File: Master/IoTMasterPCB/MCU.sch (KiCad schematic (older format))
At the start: 34 parts

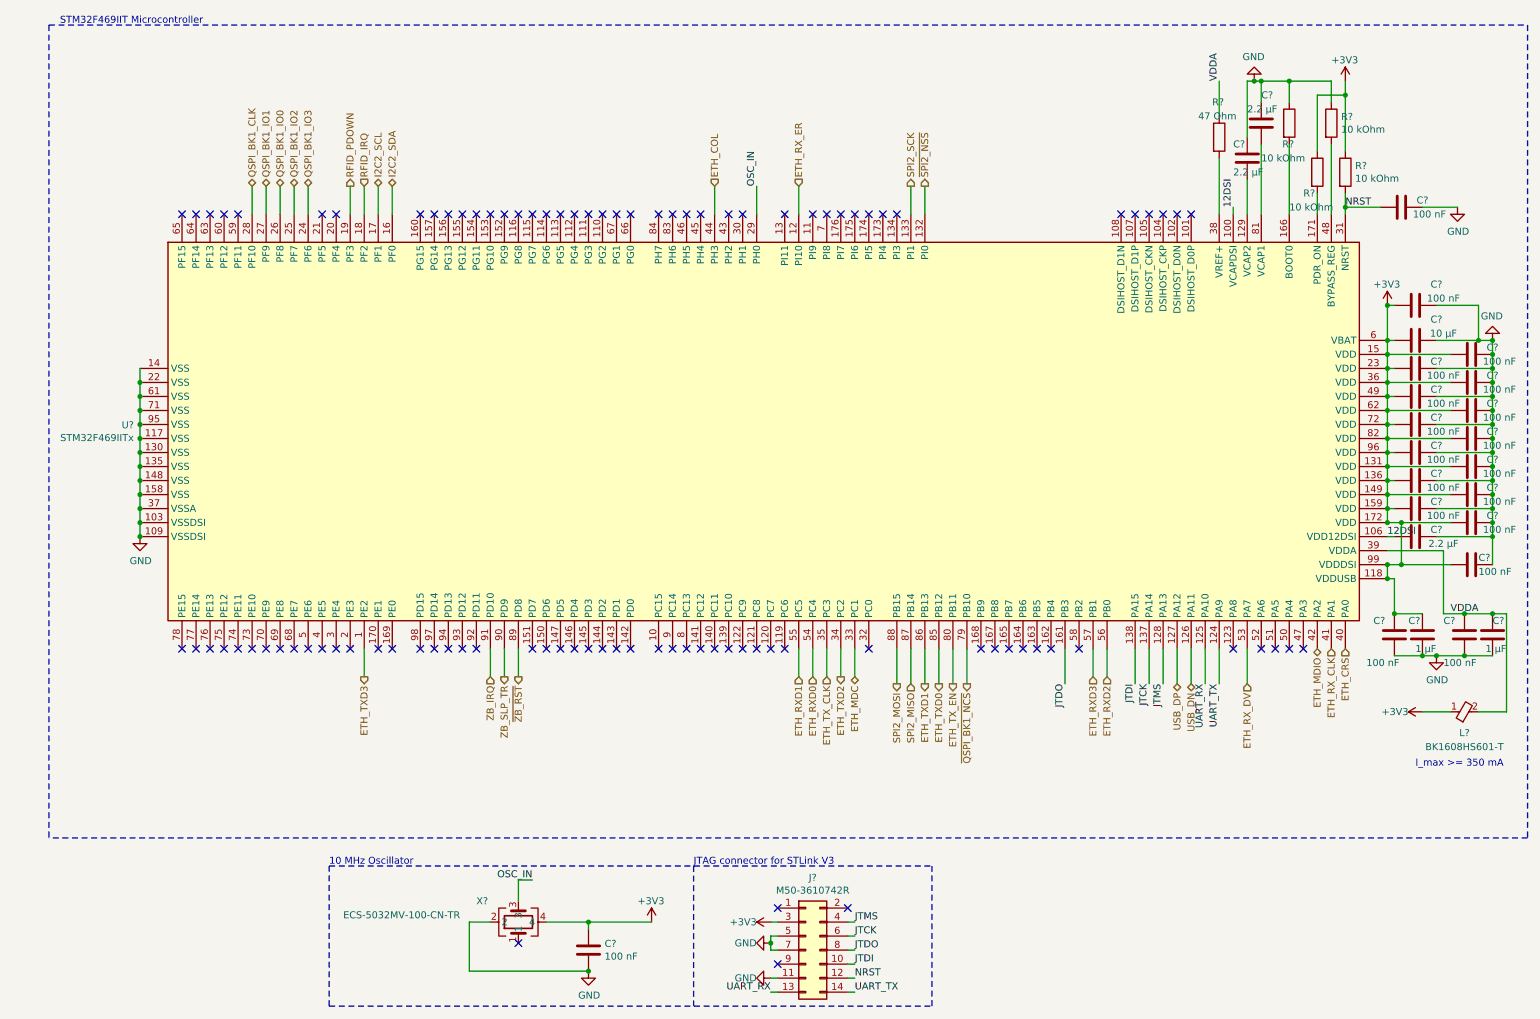
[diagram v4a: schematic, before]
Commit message: Finished RFID and Ethernet circuits.
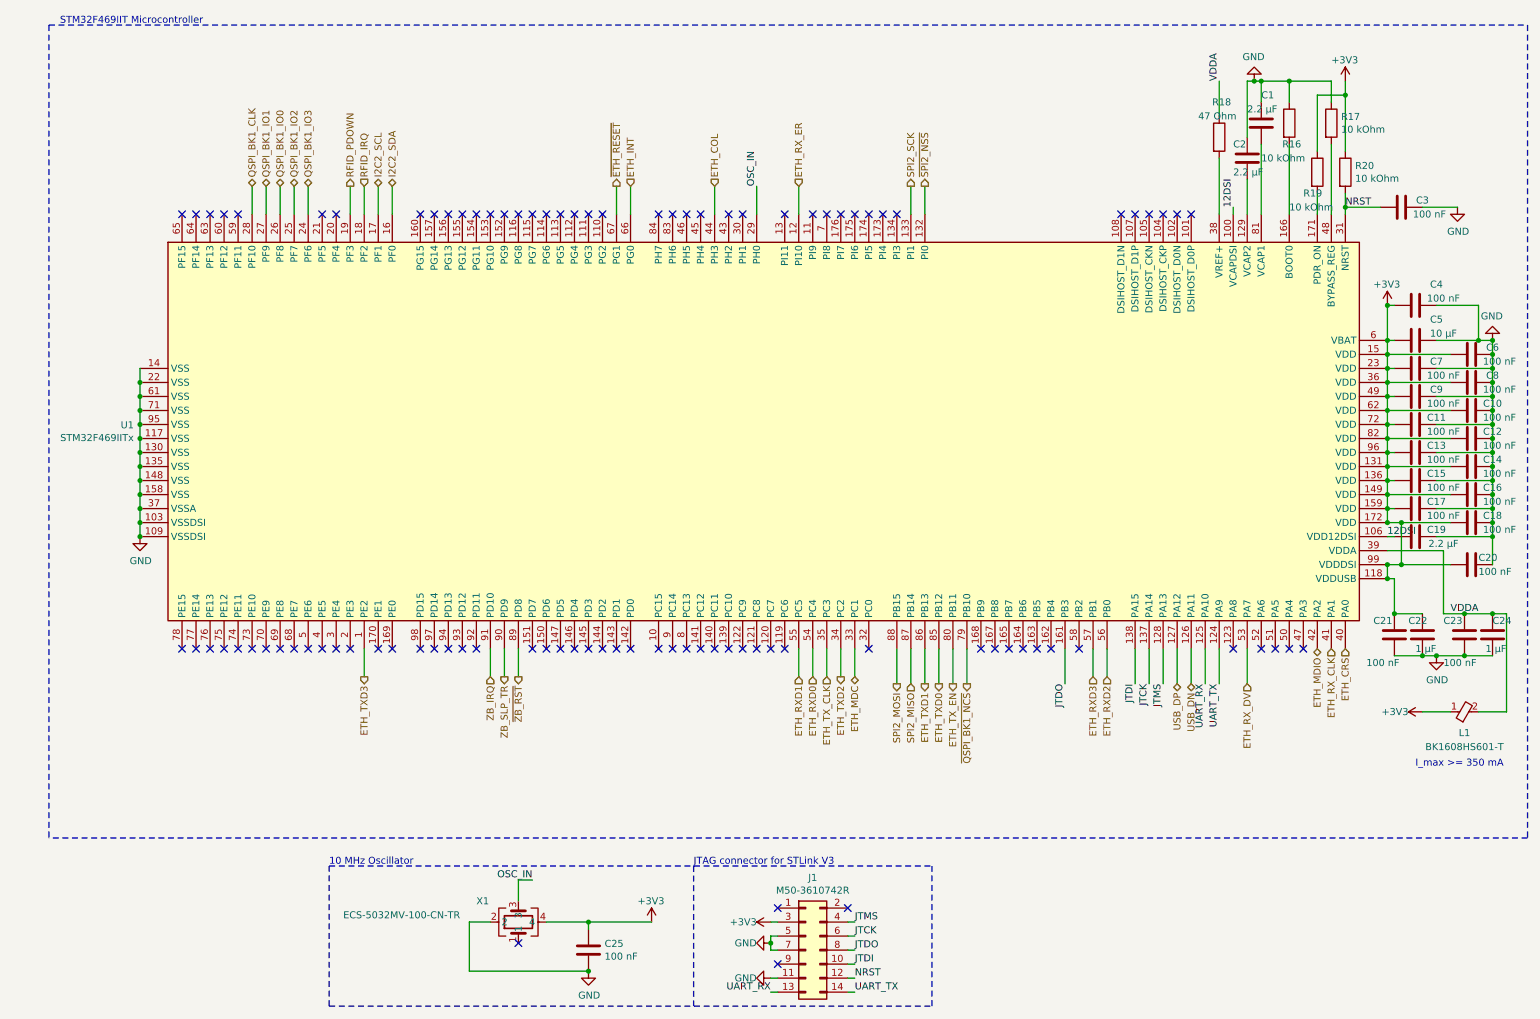
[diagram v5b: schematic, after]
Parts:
- L1: renamed from L?; Height 0.95 -> (none); Manufacturer_Name TAIYO YUDEN -> (none); Manufacturer_Part_Number BK1608HS601-T -> (none); Mouser Part Number 963-BK1608HS601-T -> (none); Mouser Price/Stock https://www.mouser.co.uk/ProductDetail/Taiyo-Yuden/BK1608HS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 -> (none)
- gave numbers to parts that had none: 33
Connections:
- net ETH_INT: now reaches U1.66 (PG0)
- net ~ETH_RESET: now reaches U1.67 (PG1)
- no-connect marks 98 -> 96

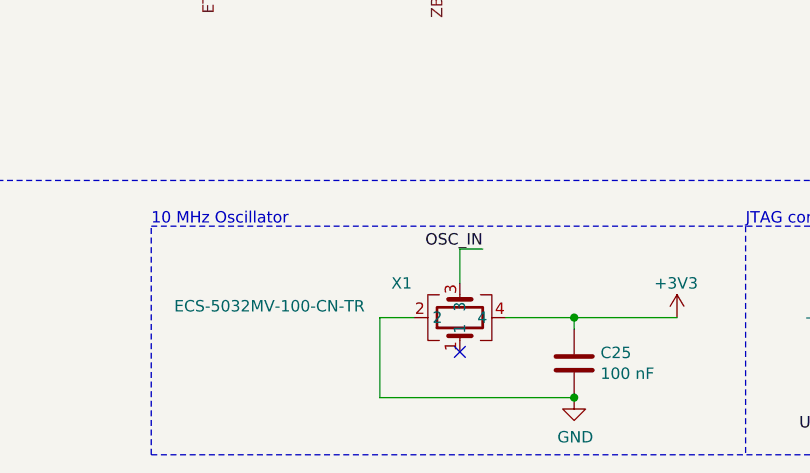
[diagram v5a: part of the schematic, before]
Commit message: Minor changes to schematic, finished placing all components, only minor fixes needed to PCB now.
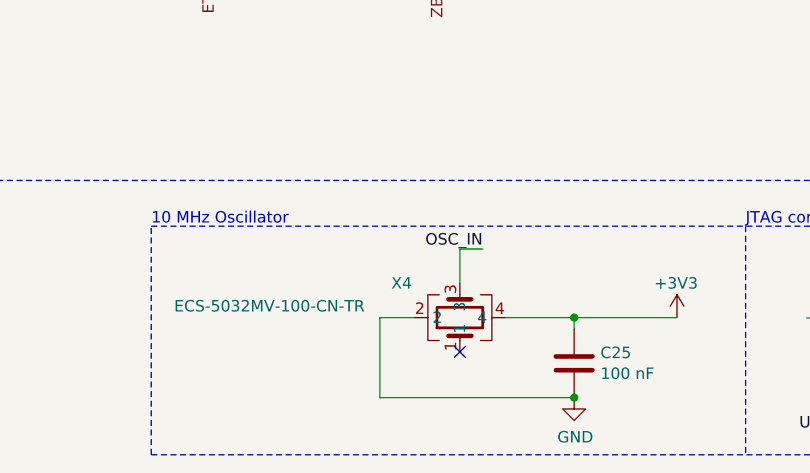
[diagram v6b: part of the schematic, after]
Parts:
- renumbered X1 to X4
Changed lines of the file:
@@
 P 3900 7250
 AR Path="/5F196B29/5FE0C4B1" Ref="X?"  Part="1"
-AR Path="/5F9E799A/5FE0C4B1" Ref="X1"  Part="1"
-F 0 "X1" V 4200 7550 50  0000 R CNN
+AR Path="/5F9E799A/5FE0C4B1" Ref="X4"  Part="1"
+F 0 "X4" V 4200 7550 50  0000 R CNN
 F 1 "ECS-5032MV-100-CN-TR" V 4100 8500 50  0000 R CNN
 F 2 "Personal_Actives:ECS5032MV250CNTR" H 5250 7350 50  0001 L CNN

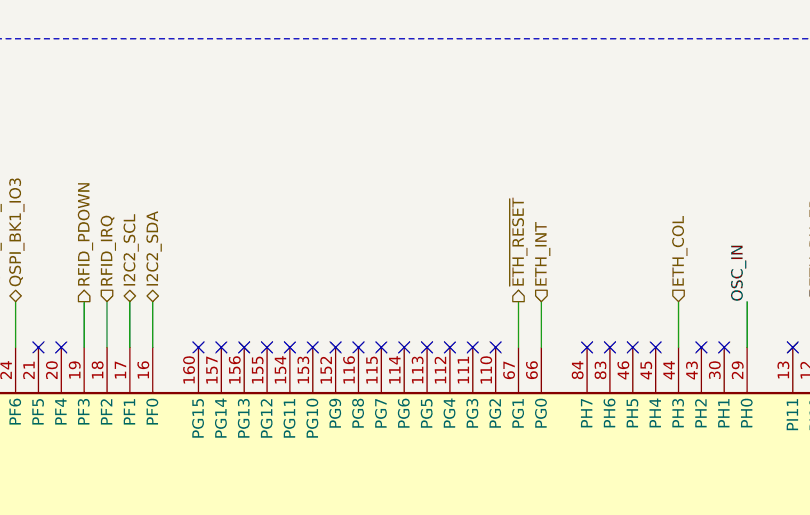
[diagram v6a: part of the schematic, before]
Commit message: Added further documentation in ReadMe. Added status LEDs to Master.
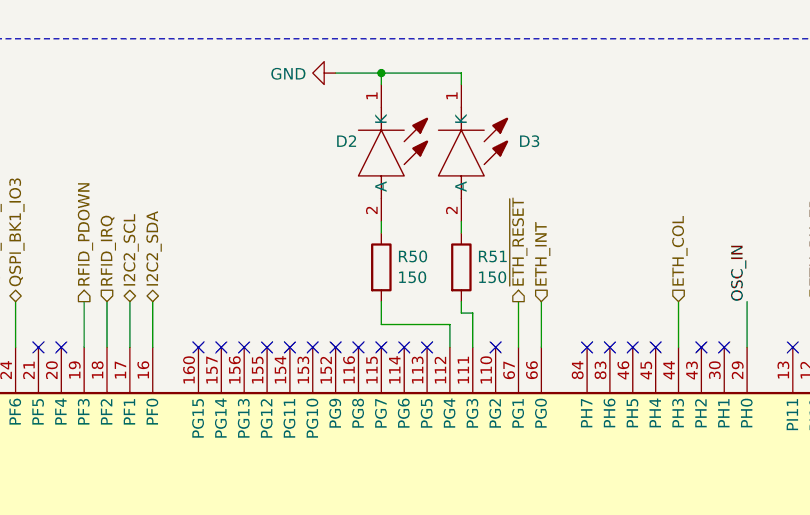
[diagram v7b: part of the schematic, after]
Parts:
- added D2: 150060SS55040, Personal_Passives:150060VS55040, symbol Personal_Passives:150060SS55040
- added D3: 150060VS55040, Personal_Passives:150060VS55040, symbol Personal_Passives:150060VS55040
- added R50, R51: 150, Resistor_SMD:R_0603_1608Metric, symbol Device:R
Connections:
- net GND: now also D2.1 (K), D3.1 (K)
- net at U1.111 (PG3): now also R51.2
- net at U1.112 (PG4): now also R50.2
- new net: D2.2 (A), R50.1
- new net: D3.2 (A), R51.1
- no-connect marks 96 -> 94
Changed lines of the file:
@@
 NoConn ~ 4000 2050
 NoConn ~ 4100 2050
-NoConn ~ 4400 2050
-NoConn ~ 4500 2050
 NoConn ~ 4900 2050
 NoConn ~ 5000 2050
@@
 NoConn ~ 8300 2050
 NoConn ~ 8200 2050
-NoConn ~ 4300 2050
 NoConn ~ 4200 2050
 NoConn ~ 3900 2050
@@
 Text HLabel 4600 1850 1    50   Output ~ 0
 ~ETH_RESET
+$Comp
+L Personal_Passives:150060SS55040 D2
+U 1 1 602A364D
+P 4000 900
+F 0 "D2" V 4250 700 50  0000 L CNN
+F 1 "150060SS55040" V 4345 1130 50  0001 L CNN
+F 2 "Personal_Passives:150060VS55040" H 4500 1050 50  0001 L BNN
+F 3 "" H 4500 950 50  0001 L BNN
+F 4 "2.4 V Red LED 1608 (0603)  SMD, Wurth Elektronik WL-SMCD 150060SS55040" H 4500 850 50  0001 L BNN "Description"
+F 5 "710-150060SS55040" H 4500 650 50  0001 L BNN "Mouser Part Number"
+F 6 "https://www.mouser.co.uk/ProductDetail/Wurth-Elektronik/150060SS55040?qs=8Aam6%252B7C6HG0AGgMR5PhFg%3D%3D" H 4500 550 50  0001 L BNN "Mouser Price/Stock"
+F 7 "Wurth Elektronik" H 4500 450 50  0001 L BNN "Manufacturer_Name"
+F 8 "150060SS55040" H 4500 350 50  0001 L BNN "Manufacturer_Part_Number"
+	1    4000 900
+	0    1    1    0
+$EndComp
+$Comp
+L Personal_Passives:150060VS55040 D3
+U 1 1 602AA6D1
+P 4350 900
+F 0 "D3" V 4600 1150 50  0000 L CNN
+F 1 "150060VS55040" V 4695 1130 50  0001 L CNN
+F 2 "Personal_Passives:150060VS55040" H 4850 1050 50  0001 L BNN
+F 3 "https://katalog.we-online.com/led/datasheet/150060VS55040.pdf" H 4850 950 50  0001 L BNN
+F 4 "LED, 150060VS55040, Wurth Elektronik WL-SMCD 573 (Typ.) nm 0603 Diffused SMD package" H 4850 850 50  0001 L BNN "Description"
+F 5 "0.5" H 4850 750 50  0001 L BNN "Height"
+F 6 "710-150060VS55040" H 4850 650 50  0001 L BNN "Mouser Part Number"
+F 7 "https://www.mouser.co.uk/ProductDetail/Wurth-Elektronik/150060VS55040?qs=8Aam6%252B7C6HEumg%252B0cJZzvA%3D%3D" H 4850 550 50  0001 L BNN "Mouser Price/Stock"
+F 8 "Wurth Elektronik" H 4850 450 50  0001 L BNN "Manufacturer_Name"
+F 9 "150060VS55040" H 4850 350 50  0001 L BNN "Manufacturer_Part_Number"
+	1    4350 900
+	0    1    1    0
+$EndComp
+Wire Wire Line
+	4400 2050 4400 1900
+Wire Wire Line
+	4400 1900 4350 1900
+Wire Wire Line
+	4000 1950 4300 1950
+Wire Wire Line
+	4300 1950 4300 2050
+NoConn ~ 4500 2050
+$Comp
+L Device:R R51
+U 1 1 602CD8C4
+P 4350 1700
+F 0 "R51" H 4420 1746 50  0000 L CNN
+F 1 "150" H 4420 1655 50  0000 L CNN
+F 2 "Resistor_SMD:R_0603_1608Metric" V 4280 1700 50  0001 C CNN
+F 3 "~" H 4350 1700 50  0001 C CNN
+	1    4350 1700
+	1    0    0    -1
+$EndComp
+$Comp
+L Device:R R50
+U 1 1 602CDD0B
+P 4000 1700
+F 0 "R50" H 4070 1746 50  0000 L CNN
+F 1 "150" H 4070 1655 50  0000 L CNN
+F 2 "Resistor_SMD:R_0603_1608Metric" V 3930 1700 50  0001 C CNN
+F 3 "~" H 4000 1700 50  0001 C CNN
+	1    4000 1700
+	1    0    0    -1
+$EndComp
+Wire Wire Line
+	4000 1950 4000 1850
+Wire Wire Line
+	4350 1900 4350 1850
+$Comp
+L power:GND #PWR01
+U 1 1 603052E3
+P 3800 850
+F 0 "#PWR01" H 3800 600 50  0001 C CNN
+F 1 "GND" V 3805 722 50  0000 R CNN
+F 2 "" H 3800 850 50  0001 C CNN
+F 3 "" H 3800 850 50  0001 C CNN
+	1    3800 850
+	0    1    1    0
+$EndComp
+Wire Wire Line
+	3800 850  4000 850
+Wire Wire Line
+	4350 850  4350 900
+Wire Wire Line
+	4000 900  4000 850
+Connection ~ 4000 850
+Wire Wire Line
+	4000 850  4350 850
+Wire Wire Line
+	4350 1550 4350 1500
+Wire Wire Line
+	4000 1550 4000 1500
 $EndSCHEMATC
